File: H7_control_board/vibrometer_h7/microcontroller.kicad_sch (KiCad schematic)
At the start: 35 parts, among them J2 GPIO_header, J201 Conn_01x04_Socket, J202 Conn_ST_STDC14, J203 TC2030-NL, Q2 BSS138, Q201 BSS138, Q202 BSS138, SW201 SW_Push, U201 STM32H723VGTx, Y201 24MHz

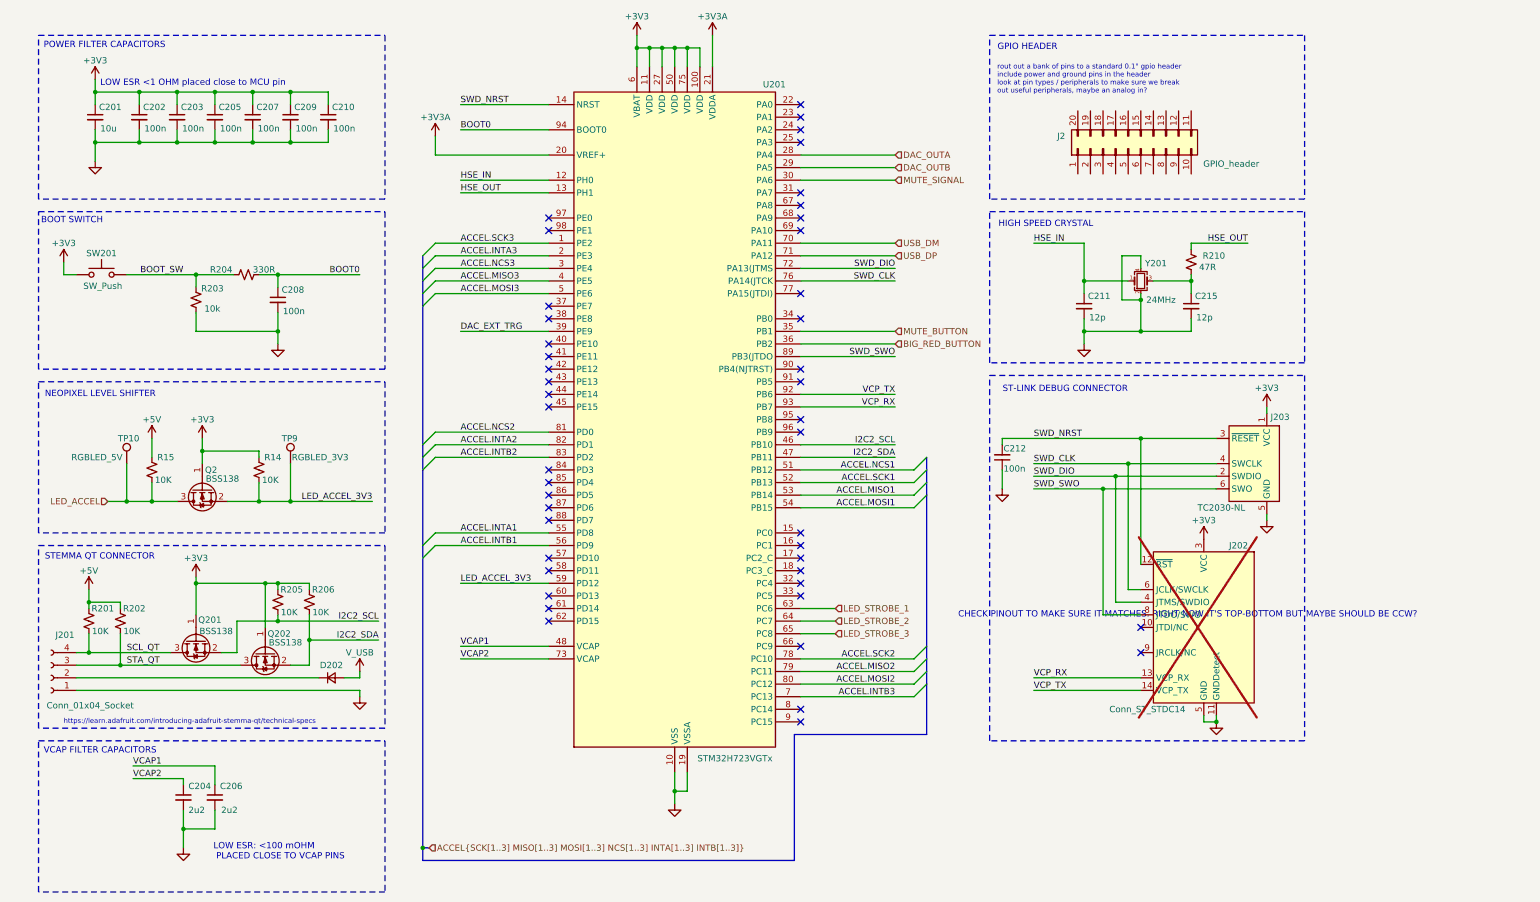
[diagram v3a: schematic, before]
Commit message: first pass at board routing
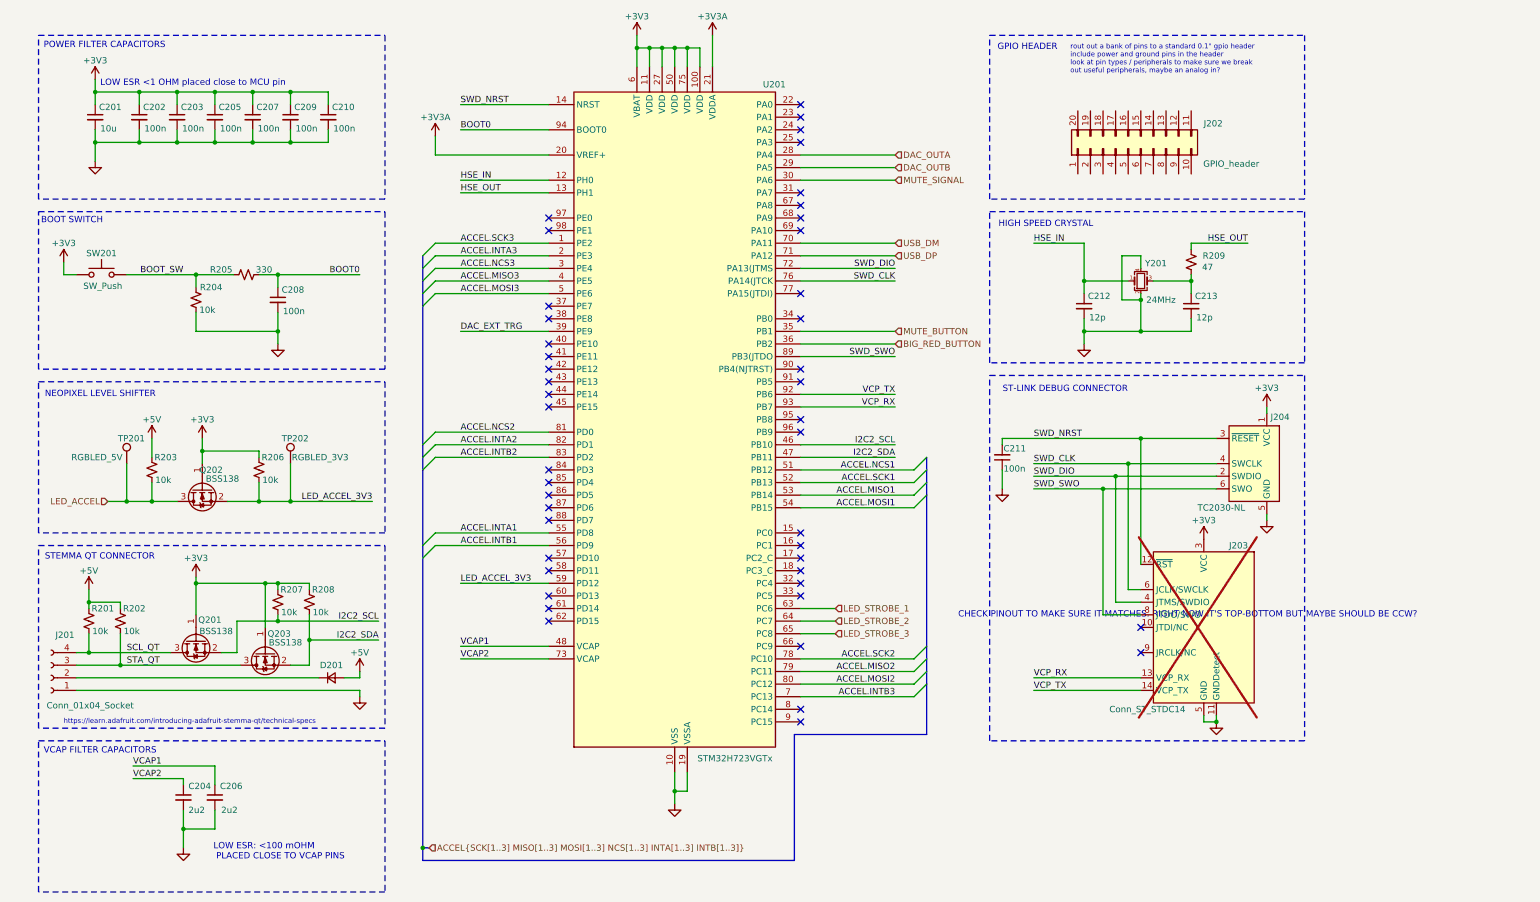
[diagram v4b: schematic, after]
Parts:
- C204, C206: LCSC (none) -> C377773
- C212: renamed from C211; footprint Capacitor_SMD:C_0603_1608Metric -> Capacitor_SMD:C_0402_1005Metric; LCSC (none) -> C1547
- C213: renamed from C215; footprint Capacitor_SMD:C_0603_1608Metric -> Capacitor_SMD:C_0402_1005Metric; LCSC (none) -> C1547
- D201: renamed from D202; value D_Small -> Schottky Diode; footprint (none) -> Diode_SMD:D_SOD-323; LCSC (none) -> C191023
- J201: footprint (none) -> Connector_JST:JST_SH_SM04B-SRSS-TB_1x04-1MP_P1.00mm_Horizontal; LCSC (none) -> C160404
- J203: renamed from J202; footprint Connector_PinHeader_1.27mm:PinHeader_2x07_P1.27mm_Vertical_SMD -> (none)
- R201, R202: value 10K -> 10k; footprint (none) -> Resistor_SMD:R_0603_1608Metric; LCSC (none) -> C25744
- R203: renamed from R15; value 10K -> 10k; footprint (none) -> Resistor_SMD:R_0603_1608Metric; LCSC (none) -> C25744
- R204: renamed from R203; footprint (none) -> Resistor_SMD:R_0603_1608Metric; LCSC (none) -> C25744
- R205: renamed from R204; value 330R -> 330; footprint (none) -> Resistor_SMD:R_0402_1005Metric; LCSC (none) -> C25104
- R206: renamed from R14; value 10K -> 10k; footprint (none) -> Resistor_SMD:R_0603_1608Metric; LCSC (none) -> C25744
- R207: renamed from R205; value 10K -> 10k; footprint (none) -> Resistor_SMD:R_0603_1608Metric; LCSC (none) -> C25744
- R208: renamed from R206; value 10K -> 10k; footprint (none) -> Resistor_SMD:R_0603_1608Metric; LCSC (none) -> C25744
- R209: renamed from R210; value 47R -> 47; footprint (none) -> Resistor_SMD:R_0603_1608Metric; LCSC (none) -> C23182
- SW201: footprint Button_Switch_SMD:SW_Push_1P1T_XKB_TS-1187A -> Button_Switch_SMD:SW_SPST_PTS645; LCSC C318884 -> C3010224
- TP201: renamed from TP10; footprint (none) -> TestPoint:TestPoint_Pad_D1.0mm
- TP202: renamed from TP9; footprint (none) -> TestPoint:TestPoint_Pad_D1.0mm
- Y201: footprint (none) -> Crystal:Crystal_SMD_2016-4Pin_2.0x1.6mm; LCSC (none) -> C2965584
- renumbered C212 to C211, J2 to J202, J203 to J204, Q2 to Q202, Q202 to Q203
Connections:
- net V_USB is gone; now on net +5V: D201.2 (A)

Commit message: lots of routing progress!!
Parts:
- removed J202: GPIO_header, symbol Connector_Generic:Conn_02x10_Counter_Clockwise
- removed J203: Conn_ST_STDC14, symbol Connector:Conn_ST_STDC14
- added J202: Conn_02x06, Connector_PinHeader_1.00mm:PinHeader_2x06_P1.00mm_Vertical_SMD, symbol Connector_Generic:Conn_02x06_Odd_Even
- TP202: value RGBLED_3V3 -> DAC TRG; footprint TestPoint:TestPoint_Pad_D1.0mm -> (none)
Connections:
- net +3V3: now also J202.1 (Pin_1)
- net BIG_RED_BUTTON: now also U201.77 (PA15(JTDI)); no longer U201.36 (PB2)
- net DAC_EXT_TRG: now also TP202.1, U201.66 (PC9); no longer U201.39 (PE9)
- net GND: now also J202.11 (Pin_11)
- net LED_ACCEL_3V3: no longer TP202.1
- net MUTE_BUTTON: now also U201.24 (PA2); no longer U201.35 (PB1)
- net MUTE_SIGNAL: now also U201.25 (PA3); no longer U201.30 (PA6)
- net VCP_RX: now also J202.4 (Pin_4)
- net VCP_TX: now also J202.2 (Pin_2)
- net ADC2_INN: now reaches U201.31 (PA7)
- net ADC2_INN: now also J202.10 (Pin_10)
- net ADC1_INP: now reaches U201.32 (PC4)
- net ADC1_INP: now also J202.8 (Pin_8)
- net ADC1_INN: now reaches U201.33 (PC5)
- net ADC1_INN: now also J202.6 (Pin_6)
- net UART_RX: now reaches U201.37 (PE7)
- net UART_RX: now also J202.9 (Pin_9)
- net UART_TX: now reaches U201.38 (PE8)
- net UART_TX: now also J202.7 (Pin_7)
- net UART_CTS: now reaches U201.40 (PE10)
- net UART_CTS: now also J202.3 (Pin_3)
- net 5V_QT: now reaches D201.1 (K), J201.2 (Pin_2)
- new net ADC2_INP: J202.12 (Pin_12), U201.30 (PA6)
- new net UART_RTS: J202.5 (Pin_5), U201.39 (PE9)
- no-connect marks 45 -> 35
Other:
- note added: "TAG CONNECT DEBUG PORT"
- note removed: "CHECK PINOUT TO MAKE SURE IT MATCHES. RIGHT NOW IT'S TOP-BOTTOM BUT MAYBE SHOULD BE CCW?"
- note removed: "ST-LINK DEBUG CONNECTOR"
- note removed: "rout out a bank of pins to a standard 0.1" gpio header include power and ground pins in the header look at pin types / peripherals to make sure we break out useful peripherals, maybe an analog in?"
- moved on the sheet: C211, J204

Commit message: zero unrouts! But still need to fix footprint for headphone jack. So 3 unrouts!
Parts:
- TP202: footprint (none) -> TestPoint:TestPoint_Pad_D1.0mm

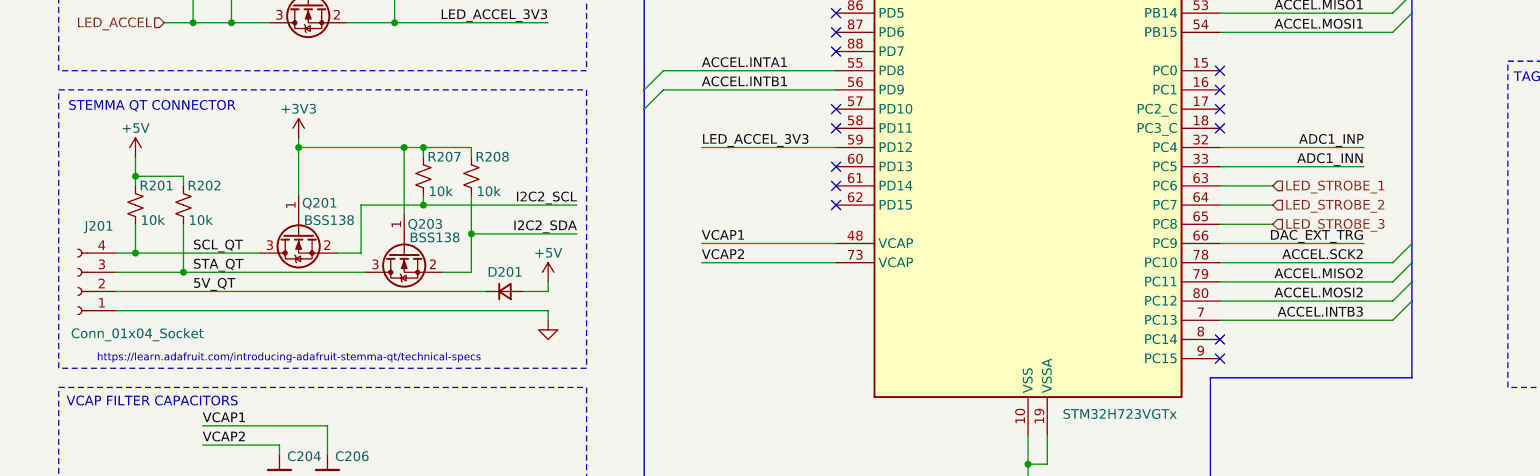
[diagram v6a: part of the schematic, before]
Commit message: cleaned up silkscreen
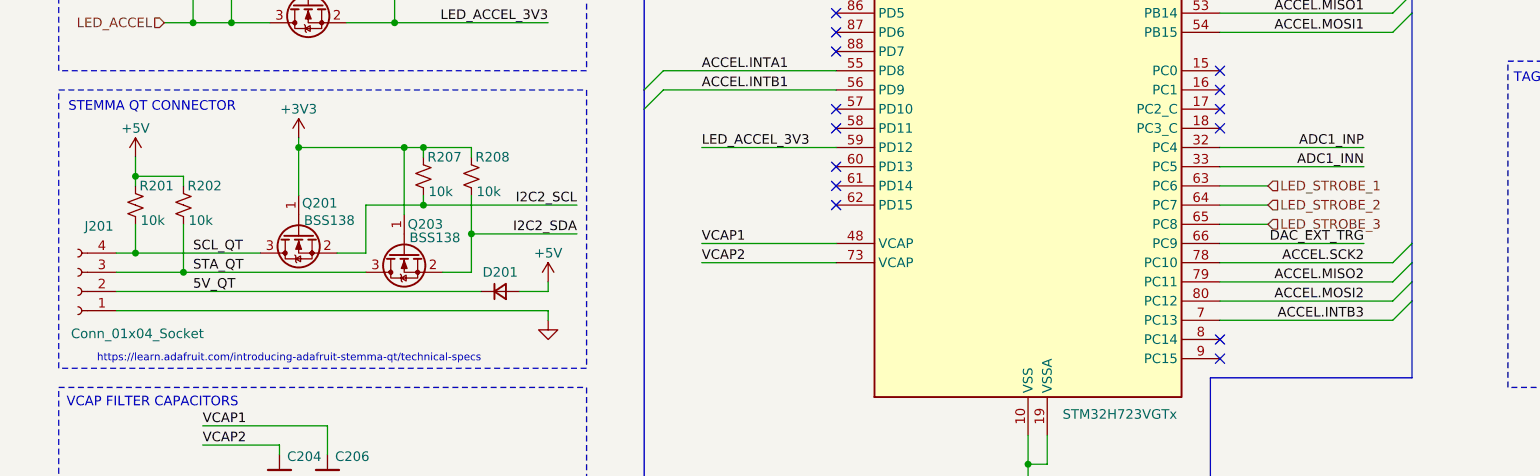
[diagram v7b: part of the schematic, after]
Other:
- moved on the sheet: D201

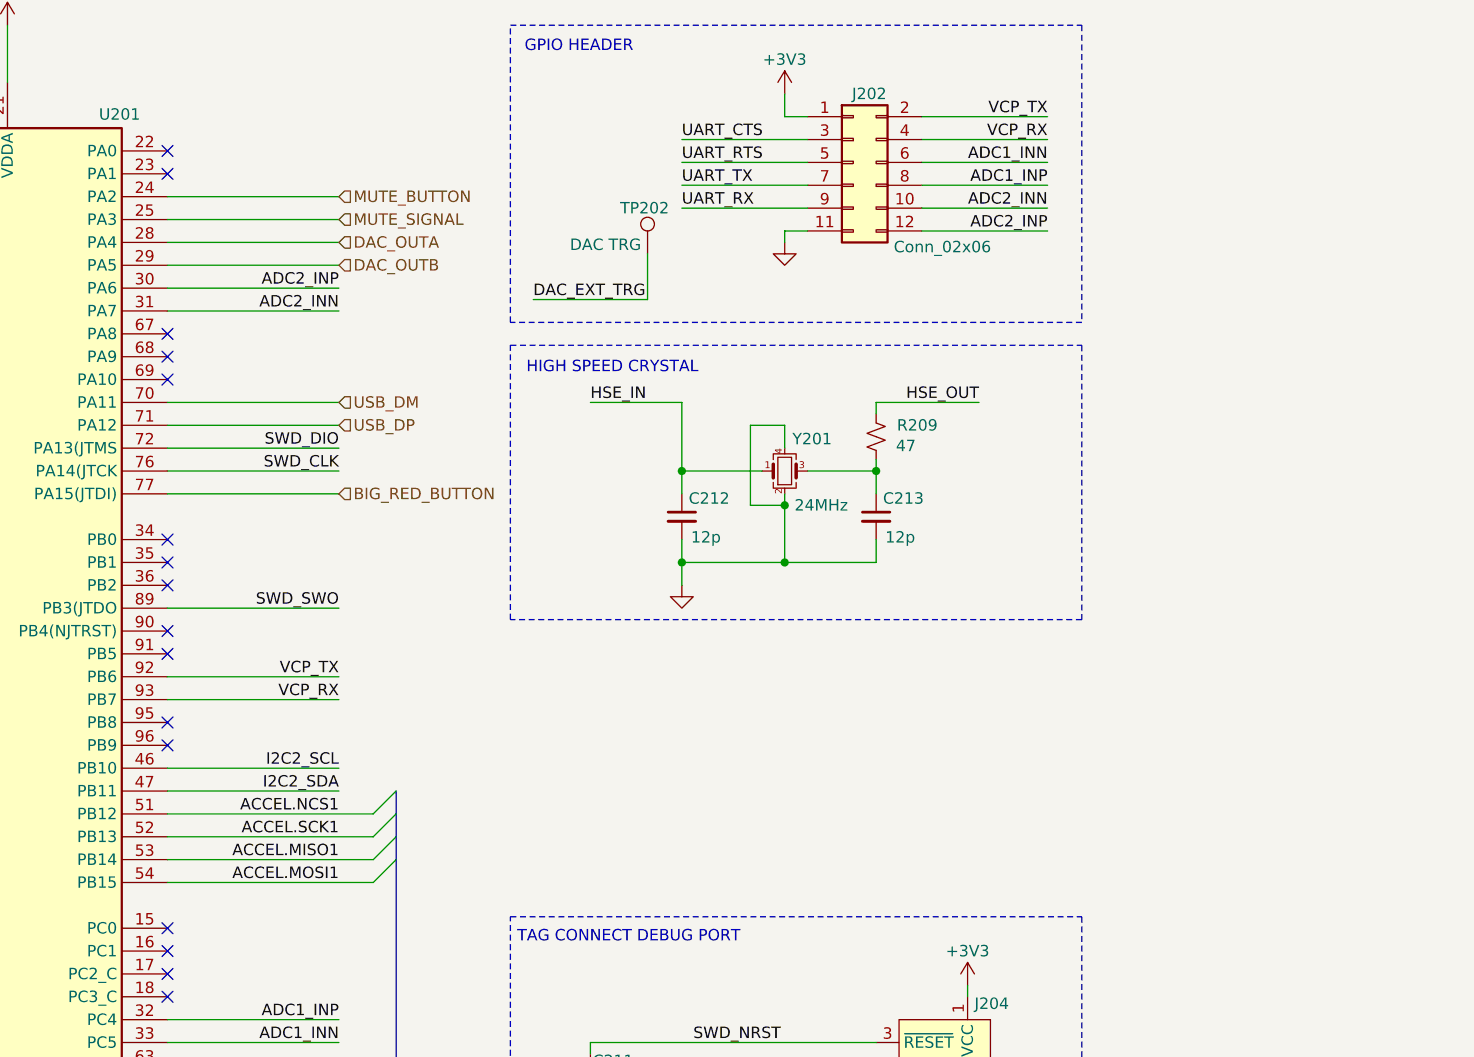
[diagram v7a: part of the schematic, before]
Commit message: added indicator leds
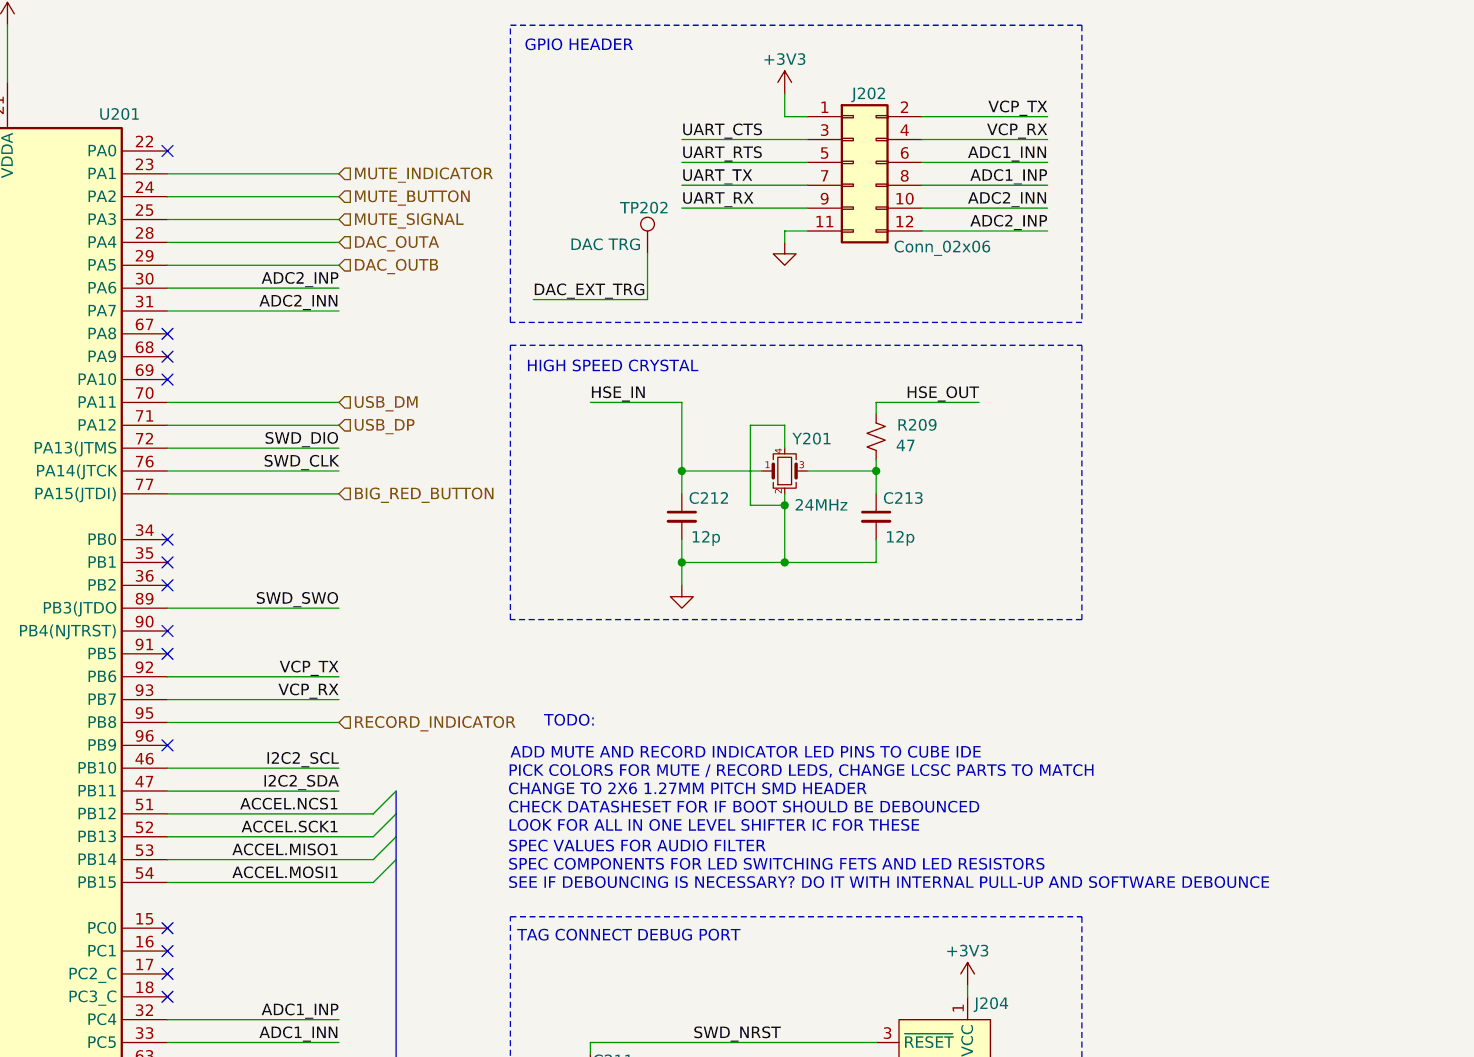
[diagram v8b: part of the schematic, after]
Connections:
- net MUTE_INDICATOR: now reaches U201.23 (PA1)
- net RECORD_INDICATOR: now reaches U201.95 (PB8)
- no-connect marks 35 -> 33
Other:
- note added: "ADD MUTE AND RECORD INDICATOR LED PINS TO CUBE IDE"
- note added: "CHANGE TO 2X6 1.27MM PITCH SMD HEADER"
- note added: "CHECK DATASHESET FOR IF BOOT SHOULD BE DEBOUNCED"
- note added: "LOOK FOR ALL IN ONE LEVEL SHIFTER IC FOR THESE"
- note added: "PICK COLORS FOR MUTE / RECORD LEDS, CHANGE LCSC PARTS TO MATCH"
- note added: "SEE IF DEBOUNCING IS NECESSARY? DO IT WITH INTERNAL PULL-UP AND SOFTWARE DEBOUNCE"
- note added: "SPEC COMPONENTS FOR LED SWITCHING FETS AND LED RESISTORS"
- note added: "SPEC VALUES FOR AUDIO FILTER"
- note added: "TODO:"
